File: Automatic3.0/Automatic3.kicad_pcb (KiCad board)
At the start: 2 copper layers, 83 parts, among them J1 CONN_01X02, J10 Encoder, J11 UART0, J12 Bluetooth, J13 Compass, J14 CONN_01X06, J15 I/O PINS, J16 CONN_01X01, J17 CONN_01X01, J18 CONN_01X01, J19 CONN_01X01, J2 CONN_02X04, J3 Motor, J4 Jumper, J5 USB_B, J6 Jumper, J7 Bluetooth, J8 Line Tracker and Proximity, J9 Reset_jumper, SW1 SW_Push, SW2 SW_Push, U1 Buck, U2 LM7809, U3 Arduino_Mega2560_Shield, U4 ATMEGA88A-PU, Y1 Crystal

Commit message: Created new schemetic for automatic
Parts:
- removed C12, C14: C, modFiles:Capacitor_Disc_Medium
- removed C13: 22, modFiles:Capacitor_Disc_Small
- removed J19: CONN_01X01, Connectors:1pin
- removed R23, R26, R27, R28, R29, R30, R31, R32, R33, R34, R35: 10k, modFiles:Resistor_small
- removed Y1: Crystal, modFiles:Crystal
- added C5: 0.1uF, modFiles:Capacitor_Disc_Medium, F.Cu at (326.6, 52.1)
- added D10: D, Diodes_THT:D_DO-27_P12.70mm_Horizontal, F.Cu at (99.8, 62.5)
- added D12: LED, modFiles:LED_D3.0mm, F.Cu at (153.2, 94.0)
- added D13: LED, modFiles:LED_D3.0mm, F.Cu at (94.7, 103.1)
- added R6: 10K, modFiles:Resistor_small, F.Cu at (122.4, 122.7)
- C1: value 1000uF -> 0.1uF; footprint modFiles:Capacitor_1000uF -> modFiles:Capacitor_Disc_Medium
- C10: value 0.1uF -> 10uF; footprint modFiles:Capacitor_Disc_Medium -> modFiles:Capacitor_10uF
- C11, C9: value 0.1uF -> 100uF; footprint modFiles:Capacitor_Disc_Medium -> modFiles:Capacitor_100uF
- C2: value 100uF -> C; footprint modFiles:Capacitor_100uF -> modFiles:Capacitor_Disc_Medium
- C3: value 10uF -> 0.1uF; footprint modFiles:Capacitor_10uF -> modFiles:Capacitor_Disc_Medium
- C4: value 100uF -> 0.1uF; footprint modFiles:Capacitor_100uF -> modFiles:Capacitor_Disc_Medium
- C7: value 22 -> C; footprint modFiles:Capacitor_Disc_Small -> modFiles:Capacitor_Disc_Medium
- C8: value 0.1uF -> 1000uF; footprint modFiles:Capacitor_Disc_Medium -> modFiles:Capacitor_1000uF
- D1: value D -> D_Zener; footprint Diodes_THT:D_DO-27_P12.70mm_Horizontal -> Diodes_THT:D_DO-35_SOD27_P7.62mm_Horizontal
- D11: footprint modFiles:Diode_Small -> Diodes_THT:D_DO-27_P12.70mm_Horizontal
- D2: footprint Diodes_THT:D_DO-27_P12.70mm_Horizontal -> modFiles:Diode_Small
- D3: value LED -> D; footprint modFiles:LED_D3.0mm -> modFiles:Diode_Small
- D4: value LED -> D_Zener; footprint modFiles:LED_D3.0mm -> Diodes_THT:D_DO-35_SOD27_P7.62mm_Horizontal
- D8: value D -> LED; footprint modFiles:Diode_Small -> modFiles:LED_D3.0mm
- D9: value D_Zener -> LED; footprint Diodes_THT:D_DO-35_SOD27_P7.62mm_Horizontal -> modFiles:LED_D3.0mm
- J1: value CONN_01X02 -> I/O PINS; footprint modFiles:Solar_Connector -> Pin_Headers:Pin_Header_Straight_1x03_Pitch2.54mm
- J10: value Encoder -> Line Tracker and Proximity
- J11: value UART0 -> Compass; footprint Pin_Headers:Pin_Header_Straight_1x02_Pitch2.54mm -> Pin_Headers:Pin_Header_Straight_1x04_Pitch2.54mm
- J12: footprint Pin_Headers:Pin_Header_Straight_1x04_Pitch2.54mm -> Pin_Headers:Pin_Header_Straight_1x06_Pitch2.54mm
- J13: value Compass -> Encoder; footprint Pin_Headers:Pin_Header_Straight_1x04_Pitch2.54mm -> modFiles:Connector_DB15
- J14: value CONN_01X06 -> Bluetooth
- J15: value I/O PINS -> Motor; footprint Pin_Headers:Pin_Header_Straight_1x03_Pitch2.54mm -> modFiles:Connector_DB15
- J16: value CONN_01X01 -> CONN_01X02; footprint Connectors:1pin -> modFiles:Solar_Connector
- J17, J18: value CONN_01X01 -> Reset_Jumper; footprint Connectors:1pin -> Pin_Headers:Pin_Header_Straight_1x03_Pitch2.54mm
- J2: value CONN_02X04 -> CONN_01X01; footprint Pin_Headers:Pin_Header_Straight_2x04_Pitch2.54mm -> Connectors:1pin
- J3: value Motor -> CONN_02X04; footprint modFiles:Connector_DB15 -> Pin_Headers:Pin_Header_Straight_2x04_Pitch2.54mm
- J4: value Jumper -> CONN_01X01; footprint Pin_Headers:Pin_Header_Straight_1x02_Pitch2.54mm -> Connectors:1pin
- J5: value USB_B -> CONN_01X01; footprint modFiles:Connector_USB -> Connectors:1pin
- J6: value Jumper -> I/O Pins; footprint Pin_Headers:Pin_Header_Straight_1x02_Pitch2.54mm -> Pin_Headers:Pin_Header_Straight_1x08_Pitch2.54mm
- J7: value Bluetooth -> USB_B; footprint Pin_Headers:Pin_Header_Straight_1x04_Pitch2.54mm -> modFiles:Connector_USB
- J8: value Line Tracker and Proximity -> CONN_01X01; footprint modFiles:Connector_DB15 -> Connectors:1pin
- J9: value Reset_jumper -> I/O Pins; footprint Pin_Headers:Pin_Header_Straight_1x03_Pitch2.54mm -> Pin_Headers:Pin_Header_Straight_1x08_Pitch2.54mm
- R1: value 1K5 -> 1
- R10: footprint Resistors_THT:R_Axial_DIN0207_L6.3mm_D2.5mm_P10.16mm_Horizontal -> modFiles:Resistor_small
- R14: value 10K -> 1K5
- R15, R16, R18, R20: value 10K -> 1K
- R17, R19: value 10K -> 330; footprint modFiles:Resistor_small -> Resistors_THT:R_Axial_DIN0207_L6.3mm_D2.5mm_P10.16mm_Horizontal
- R2, R4: value 1K -> 10K
- R21: value 10K -> 10k
- R22: value 150 -> 10k
- R3: value 330 -> 10K
- R5: value 1 -> 10K
- R8: value 10k -> 10K
- SW1, SW2: value SW_Push -> Reset
- U1: value Buck -> Arduino_Mega2560_Shield; footprint modFiles:Buck_Regulator -> modFiles:Arduino_Mega2560_Shield
- U2: value LM7809 -> Arduino_Mega2560_Shield; footprint modFiles:Voltage_Regulators -> modFiles:Arduino_Mega2560_Shield
- U3: value Arduino_Mega2560_Shield -> Buck; footprint modFiles:Arduino_Mega2560_Shield -> modFiles:Buck_Regulator
- U4: value ATMEGA88A-PU -> LM7809; footprint modFiles:DIP-28 -> modFiles:Voltage_Regulators
- moved C3 243.1 mm to (338.3, 49.8), turned to 0 degrees
- moved C2 233.9 mm to (338.3, 58.4), turned to 0 degrees
- moved C1 224.2 mm to (326.9, 42.4), turned to 0 degrees
- moved R1 206.8 mm to (294.9, 15.0), turned to 0 degrees
- moved J1 189.5 mm to (272.5, 18.0), turned to 0 degrees
- moved C4 181.8 mm to (336.0, 36.3), turned to 0 degrees
- moved C7 177.9 mm to (338.3, 67.6)
- moved J8 141.1 mm to (266.7, 40.9)
- moved C6 138.5 mm to (335.5, 42.4), turned to 0 degrees
- moved J18 128.9 mm to (89.7, 85.1), turned to 0 degrees
- moved J5 114.9 mm to (278.9, 31.0), turned to 0 degrees
- moved J4 109.4 mm to (267.5, 29.5)
- moved J17 100.0 mm to (158.0, 75.7), turned to 0 degrees
- moved R17 93.4 mm to (109.2, 109.5), turned to 0 degrees
- moved D9 92.6 mm to (103.4, 67.6)
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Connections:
- C1 pad 1: /12VV -> GND
- C1 pad 2: GND -> +5V
- C10 pad 1: GND -> +9V
- C10 pad 2: /12VVD -> GND
- C11 pad 1: +9V -> +5V
- C2 pad 1: Net-(C2-Pad1) -> /RESET2
- C3 pad 1: +9V -> GND
- C3 pad 2: GND -> +5V
- C6 pad 1: GND -> +9V
- C6 pad 2: +5V -> GND
- C7 pad 1: Net-(C7-Pad1) -> GND
- C7 pad 2: GND -> /RESET
- C8 pad 1: GND -> /12VV
- C8 pad 2: +5V -> GND
- C9 pad 1: +5V -> Net-(C9-Pad1)
- D1 pad 1: Net-(C2-Pad1) -> /TX2
- D1 pad 2: Net-(D1-Pad2) -> GND
- D11 pad 1: /12VVD -> /12VV
- D11 pad 2: /12VV -> Net-(D11-Pad2)
- D2 pad 1: /12VV -> +5V
- D2 pad 2: /Sheet5ADE4B1B/12led -> +5V
- D3 pad 1: GND -> /12VVD
- D3 pad 2: Net-(D3-Pad2) -> /12VV
- D4 pad 1: GND -> /TX3
- D4 pad 2: Net-(D4-Pad2) -> GND
- D8 pad 1: +5V -> GND
- D8 pad 2: +5V -> Net-(D8-Pad2)
- D9 pad 1: /TX2 -> GND
- D9 pad 2: GND -> Net-(D9-Pad2)
- F1 pad 1: Net-(D1-Pad2) -> Net-(D10-Pad2)
- F2 pad 1: /Sheet5ADE4B1B/12led -> Net-(D11-Pad2)
- J1 pad 1: +12V -> /PB5
- J1 pad 2: GND -> /PB6
- J10 pad 1: /INT2 -> /PC5
- J10 pad 10: /INT4 -> GND
- J10 pad 11: /INT5 -> /12VVD
- J10 pad 12: GND -> /12VVD
- J10 pad 13: +5V -> /JP2
- J10 pad 14: +5V -> /PR1
- J10 pad 15: /PA5 -> /PR2
- J10 pad 2: /INT1 -> /PC7
- J10 pad 3: /INT0 -> /PC6
- J10 pad 4: /PA4 -> /PC4
- J10 pad 5: /PA2 -> /PC2
- J10 pad 6: /PA0 -> /PC0
- J10 pad 7: /PA1 -> /PC1
- J10 pad 8: /PA3 -> /PC3
- J10 pad 9: /INT3 -> /JP1
- J11 pad 1: /TX0 -> +5V
- J11 pad 2: /RX0 -> GND
- J12 pad 1: +5V -> Net-(J12-Pad1)
- J12 pad 2: GND -> +5V
- J12 pad 3: /RX3 -> GND
- J12 pad 4: /TX3 -> /RX2
- J13 pad 1: +5V -> /INT0
- J13 pad 2: GND -> /INT5
- J13 pad 3: Net-(J13-Pad3) -> /INT4
- J13 pad 4: Net-(J13-Pad4) -> /INT3
- J14 pad 2: Net-(J14-Pad2) -> +5V
- J14 pad 3: Net-(J14-Pad3) -> GND
- J14 pad 4: GND -> /RX3
- J14 pad 5: +5V -> /TX3
- J14 pad 6: /RESET2 -> Net-(J14-Pad6)
- J15 pad 1: /PB5 -> /OC5C
- J15 pad 2: /PB6 -> /OC5B
- J15 pad 3: /PB7 -> /PK0
- J16 pad 1: Net-(J16-Pad1) -> +12V
- J17 pad 1: Net-(J17-Pad1) -> /5VV
- J18 pad 1: Net-(J18-Pad1) -> /5VV
- J2 pad 1: +5V -> Net-(J2-Pad1)
- J3 pad 1: /PK7 -> +5V
- J3 pad 2: /PK6 -> GND
- J3 pad 3: /PK5 -> +5V
- J3 pad 4: /PK4 -> GND
- J3 pad 5: /PK3 -> +5V
- J3 pad 6: /PK2 -> GND
- J3 pad 7: /PK1 -> +5V
- J3 pad 8: /OC4A -> GND
- J6 pad 2: /TX2 -> Net-(J6-Pad2)
- J7 pad 1: +5V -> Net-(J7-Pad1)
- J7 pad 2: GND -> /TX3
- J7 pad 3: /RX2 -> /RX3
- J7 pad 4: /TX2 -> GND
- J8 pad 1: /JP1 -> Net-(J8-Pad1)
- J9 pad 1: GND -> Net-(J9-Pad1)
- J9 pad 3: /3V3 -> Net-(J9-Pad3)
- R1 pad 1: Net-(D3-Pad2) -> GND
- R1 pad 2: /Sheet5ADE4B1B/12led -> GND
- R10 pad 1: +5V -> /INT4
- R10 pad 2: /PA0 -> +5V
- R11 pad 1: /INT1 -> +5V
- R11 pad 2: +5V -> /PA4
- R12 pad 1: +5V -> /INT5
- R12 pad 2: /PA1 -> +5V
- R13 pad 1: /INT2 -> +5V
- R13 pad 2: +5V -> /PA5
- R14 pad 1: +5V -> Net-(D5-Pad2)
- R14 pad 2: /PA2 -> +12V
- R15 pad 1: Net-(J9-Pad2) -> Net-(D6-Pad2)
- R15 pad 2: /RESET -> +9V
- R16 pad 1: /INT3 -> Net-(D7-Pad2)
- R16 pad 2: +5V -> +9V
- R17 pad 1: +5V -> Net-(D8-Pad2)
- R17 pad 2: /PA3 -> +5V
- R18 pad 1: /INT4 -> Net-(D9-Pad2)
- R18 pad 2: +5V -> /12VV
- R19 pad 1: +5V -> Net-(D12-Pad2)
- R19 pad 2: /PA4 -> /5VV
- R2 pad 1: Net-(D4-Pad2) -> /INT0
- R2 pad 2: +9V -> +5V
- R20 pad 1: /INT5 -> Net-(D13-Pad2)
- R20 pad 2: +5V -> /5VV
- R21 pad 1: +5V -> Net-(J17-Pad2)
- R21 pad 2: /PA5 -> /RESET1
- R22 pad 1: Net-(D7-Pad2) -> Net-(J18-Pad2)
- R22 pad 2: /3V3 -> /RESET2
- R3 pad 1: Net-(D5-Pad2) -> +5V
- R3 pad 2: +5V -> /PA0
- R4 pad 1: Net-(D6-Pad2) -> /INT1
- R4 pad 2: /12VV -> +5V
- R5 pad 1: GND -> +5V
- R5 pad 2: GND -> /PA1
- R7 pad 2: /RESET2 -> /PA2
- R8 pad 1: +5V -> /INT3
- R8 pad 2: Net-(J13-Pad4) -> +5V
- R9 pad 1: /INT0 -> +5V
- R9 pad 2: +5V -> /PA3
- SW1 pad 2: /RESET2 -> /RESET1
- SW2 pad 2: /RESET -> /RESET2
- U1 pad 3: +5V -> /INT5
- U1 pad 4: GND -> Net-(U1-Pad4)
- U2 pad 1: Net-(C2-Pad1) -> Net-(U2-Pad1)
- U2 pad 2: GND -> /INT4
- U2 pad 3: +9V -> /INT
- U3 pad 1: /TX0 -> /12VV
- U3 pad 2: /INT4 -> GND
- U3 pad 3: /INT5 -> +5V
- U4 pad 1: /RESET2 -> Net-(C9-Pad1)
- U4 pad 2: Net-(R28-Pad2) -> GND
- U4 pad 3: Net-(R29-Pad2) -> +9V
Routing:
- net /JP2: track 106.7 -> 0.86 mm, vias 2 -> 0
- net +5V: track 222.7 -> 120.4 mm
- net /12VVD: track 44.4 -> 127.7 mm
- net /RX2: track 73.2 -> 0.00 mm
- net /TX2: track 72.8 -> 0.00 mm
- net GND: track 78.0 -> 8.44 mm, vias 2 -> 0
- net /JP1: track 11.8 -> 80.8 mm
- net /PB0: track 64.7 -> 0.00 mm
- net /5VV: track 0.00 -> 53.9 mm
- net /INT0: track 14.4 -> 67.6 mm
- net /PA0: track 18.6 -> 69.5 mm
- net /RESET2: track 66.0 -> 19.4 mm
- net /PK0: track 0.00 -> 44.7 mm
- net /PA5: track 32.8 -> 73.5 mm
- net /PC5: track 0.00 -> 36.1 mm, vias 0 -> 2
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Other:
- net class Default: clearance 0.25 -> 0.2; trace_width 1 -> 0.25; via_dia 2.1 -> 0.6; via_drill 0.8 -> 0.4
- rule trace_clearance: 0.25 -> 0.2
- board text removed: "4A K1 K2 K3 K4 K5 K6 K7"
- board text removed: "5V"
- board text removed: "9V"
- board text removed: "A3 A1 A0 A2 A4 I0 I1 I2"
- board text removed: "A5 V V G I5 I4 I3"
- board text removed: "ABU ROBOCON 2018"
- board text removed: "ABU ROBOCON 2018 AUTOMATIC BASE"
- board text removed: "ANT"
- board text removed: "ARDUINO RESET"
- board text removed: "ATMEGA RESET"
- board text removed: "B0 G G G 5A 5C 5B"
- board text removed: "B7 B6 B5"
- board text removed: "BUCK"
- board text removed: "DO--D7 , B0,B1 F0--F7 , G1,D7"
- board text removed: "G R2 T2 -"
- board text removed: "MEGA"
- board text removed: "R2 G G G V V V"
- board text removed: "RST VCC GND SCK MISO MOSI"
- board text removed: "T2 R2 G V"
- board text removed: "T2 R3 T3 G J2 P1 P2 J1"
- board text removed: "T3"
- board text removed: "V G CL DA"
- board text removed: "V R G"

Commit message: Modified the automatic circuit
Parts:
- removed C4: 0.1uF, modFiles:Capacitor_Disc_Medium
- removed J1: I/O PINS, Pin_Headers:Pin_Header_Straight_1x03_Pitch2.54mm
- added C12: 104, modFiles:Capacitor_Disc_Medium, F.Cu at (138.5, 110.5)
- added C15: 104, modFiles:Capacitor_Disc_Medium, F.Cu at (58.1, 77.0)
- added C16: 104, modFiles:Capacitor_Disc_Medium, F.Cu at (139.8, 85.6)
- added C17: 104, modFiles:Capacitor_Disc_Medium, F.Cu at (83.6, 143.8)
- added R23: 10k, modFiles:Resistor_small, F.Cu at (150.5, 77.4)
- added R24: 10k, modFiles:Resistor_small, F.Cu at (153.9, 77.3)
- C1, C3, C5, C6: value 0.1uF -> 104
- C2, C7: value C -> 104
- D12, D13, D8: value LED -> LED_5V
- D5: value LED -> LED_12V
- D6, D7: value LED -> LED_9V
- D9: value LED -> LED_BUCK
- J3: value CONN_02X04 -> GND VCC
- R17, R19: footprint Resistors_THT:R_Axial_DIN0207_L6.3mm_D2.5mm_P10.16mm_Horizontal -> modFiles:Resistor_small
- moved C3 277.2 mm to (61.5, 63.8), turned to 180 degrees
- moved C2 257.7 mm to (84.5, 102.9), turned to 180 degrees
- moved J5 257.3 mm to (43.5, 134.8)
- moved J8 222.5 mm to (44.3, 39.6)
- moved C5 221.7 mm to (124.8, 143.7), turned to 270 degrees
- moved C7 215.5 mm to (123.0, 59.9), turned to 180 degrees
- moved C1 208.1 mm to (121.1, 73.4), turned to 180 degrees
- moved C6 194.7 mm to (142.7, 69.8), turned to 270 degrees
- moved R1 169.5 mm to (158.3, 115.3)
- moved J2 144.6 mm to (168.3, 135.2)
- moved J4 100.5 mm to (167.5, 39.9)
- moved R16 42.5 mm to (123.3, 76.8), turned to 180 degrees
- moved J3 41.2 mm to (125.9, 93.6), turned to 180 degrees
- moved R19 38.0 mm to (139.3, 72.0)
- moved D7 38.0 mm to (131.0, 75.6)
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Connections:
- net /INT3 renamed /SINT3
- net /INT4 renamed /SINT4
- C1 pad 2: +5V -> +9V
- C2 pad 1: /RESET2 -> +5V
- C3 pad 2: +5V -> /RESET2
- C6 pad 1: +9V -> +5V
- C7 pad 2: /RESET -> /RESET1
- D4 pad 1: /TX3 -> /TX1
- J13 pad 1: /INT0 -> /INT2
- J13 pad 5: /INT2 -> /SINT2
- J13 pad 6: /INT1 -> /SINT5
- J14 pad 4: /RX3 -> /INT2
- J14 pad 5: /TX3 -> /TX1
- J2 pad 1: Net-(J2-Pad1) -> GND
- J4 pad 1: Net-(J4-Pad1) -> GND
- J5 pad 1: Net-(J5-Pad1) -> GND
- J7 pad 2: /TX3 -> /RX3
- J7 pad 3: /RX3 -> /TX3
- J8 pad 1: Net-(J8-Pad1) -> GND
- R2 pad 1: /INT0 -> /INT2
- R4 pad 1: /INT1 -> /SINT5
- R6 pad 1: /INT2 -> /SINT2
- U1 pad 18: Net-(U1-Pad18) -> /TX1
- U1 pad 19: Net-(U1-Pad19) -> /INT2
- U2 pad 10: Net-(U2-Pad10) -> /INT
- U2 pad 19: /INT2 -> /SINT2
- U2 pad 3: /INT -> /SINT5
- U2 pad GND5: Net-(U2-PadGND5) -> GND
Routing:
- net +5V: track 120.4 -> 374.7 mm, vias 0 -> 2
- net GND: track 8.44 -> 200.6 mm
- net /SDA: track 0.74 -> 105.2 mm, vias 0 -> 2
- net /SCL: track 0.00 -> 87.2 mm
- net +9V: track 61.1 -> 138.2 mm, vias 0 -> 2
- net /INT2: track 36.0 -> 110.9 mm
- net /JP2: track 0.86 -> 69.5 mm, vias 0 -> 2
- net /INT0: track 67.6 -> 0.00 mm
- net /SINT5: track 0.00 -> 67.0 mm
- net /TX1: track 0.00 -> 57.9 mm
- net /RX2: track 0.00 -> 47.5 mm
- net /INT: track 28.3 -> 71.0 mm
- net /SINT2: track 0.00 -> 36.0 mm
- net /INT1: track 32.9 -> 0.00 mm
- net /TX2: track 0.00 -> 25.3 mm
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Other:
- board text added: "#MASTER"
- board text added: "#SLAVE"
- board text added: "- R3 T3 G"
- board text added: "A1 A3 5V 5V G A5 A0"
- board text added: "A2 A4 I5 I2 I3 I4 MI5 MI2"
- board text added: "ABU_ROBOCON_2018"
- board text added: "ANT"
- board text added: "Automatic Base"
- board text added: "BUCK_FUSE"
- board text added: "C3 C1 C0 C2 C4 C6 C7 C5"
- board text added: "F0 F1 F2 F3 F4 F5 F6 F7"
- board text added: "K5 K4 K3 K2 K1 K0 5B 5C"
- board text added: "K7 K6 G-G-G 4A 5A"
- board text added: "LED BUCK"
- board text added: "MEGA_FUSE"
- board text added: "P2 P1 J2 12 12 G J1"
- board text added: "POWER"
- board text added: "RESET"
- board text added: "TX1 RX1 GND VCC"
- board text added: "TX2 RX2 GND VCC"
- board text added: "V R G"
- board text added: "VCC GND SCL SDA"

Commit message: modified the automatic circuit
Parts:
- removed J3: GND VCC, Pin_Headers:Pin_Header_Straight_2x04_Pitch2.54mm
- added D14: LED, modFiles:LED_D3.0mm, F.Cu at (166.3, 47.7)
- added D15: D_Zener, Diodes_THT:D_DO-35_SOD27_P7.62mm_Horizontal, F.Cu at (92.1, 94.5)
- added D16: LED, modFiles:LED_D3.0mm, F.Cu at (168.2, 52.7)
- added D17: LED, modFiles:LED_D3.0mm, F.Cu at (164.1, 52.8)
- added J1: CONN_02X05, Pin_Headers:Pin_Header_Straight_2x05_Pitch2.54mm, F.Cu at (123.3, 84.4)
- added J19: Bluetooth, Pin_Headers:Pin_Header_Straight_1x06_Pitch2.54mm, F.Cu at (94.8, 107.5)
- added R25: 1, modFiles:Resistor_small, F.Cu at (84.0, 99.3)
- added R26: 1, modFiles:Resistor_small, F.Cu at (84.3, 109.0)
- added R27: 1, modFiles:Resistor_small, F.Cu at (121.7, 106.9)
- added R28: R, modFiles:Resistor_small, F.Cu at (169.7, 57.9)
- added R29: R, modFiles:Resistor_small, F.Cu at (166.5, 57.9)
- added R30: R, modFiles:Resistor_small, F.Cu at (163.5, 57.9)
- D7: value LED_9V -> LED
- moved R1 81.8 mm to (94.4, 64.2), turned to 270 degrees
- moved R4 29.0 mm to (96.4, 87.2)
- moved D1 28.2 mm to (127.5, 112.3)
- moved C16 17.2 mm to (131.8, 100.9), turned to 270 degrees
- moved D4 14.3 mm to (153.9, 95.6), turned to 270 degrees
- moved C12 13.5 mm to (149.6, 102.7), turned to 90 degrees
- moved J14 12.8 mm to (146.4, 101.3)
- moved J12 8.48 mm to (135.7, 101.4)
- moved R22 6.61 mm to (63.6, 71.6)
- moved D3 6.29 mm to (70.0, 101.8)
- moved R17 6.19 mm to (75.9, 103.6)
- moved R15 5.83 mm to (59.8, 88.3)
- moved D8 5.49 mm to (79.1, 95.4), turned to 0 degrees
- moved C2 5.07 mm to (80.0, 100.5)
- moved C15 4.77 mm to (54.1, 74.5), turned to 270 degrees
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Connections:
- D4 pad 1: /TX1 -> /TX0
- J14 pad 4: /INT2 -> /RX0
- J14 pad 5: /TX1 -> /TX0
- R1 pad 1: GND -> /12VV
- R1 pad 2: GND -> /INT
- U1 pad A15: Net-(U1-PadA15) -> /JP2
- U1 pad A8: /JP2 -> /INT
- U2 pad 14: Net-(U2-Pad14) -> /STX3
- U2 pad 15: Net-(U2-Pad15) -> /SRX3
- U2 pad 16: Net-(U2-Pad16) -> /RX2
- U2 pad 17: Net-(U2-Pad17) -> /TX2
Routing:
- net GND: track 200.6 -> 303.6 mm
- net /TX2: track 25.3 -> 111.9 mm, vias 0 -> 2
- net /TX1: track 57.9 -> 0.00 mm
- net /INT2: track 110.9 -> 73.2 mm
- net /RX2: track 47.5 -> 82.8 mm, vias 0 -> 2
- net +5V: track 374.7 -> 405.1 mm, vias 2 -> 4
- net /12VV: track 62.6 -> 86.1 mm
- net /RX0: track 0.00 -> 19.1 mm
- net /JP2: track 69.5 -> 50.6 mm
- net /TX0: track 0.00 -> 18.5 mm
- net /INT: track 71.0 -> 53.1 mm
- net +9V: track 138.2 -> 122.2 mm
- net /5VV: track 64.4 -> 49.9 mm
- net Net-(R28-Pad2): track 0.00 -> 12.4 mm
- net Net-(D14-Pad2): track 0.00 -> 11.9 mm
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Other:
- board text added: "Bluetooth"
- board text added: "TX3 RX3 GND VCC"
- board text added: "UART0"
- board text added: "UART2"

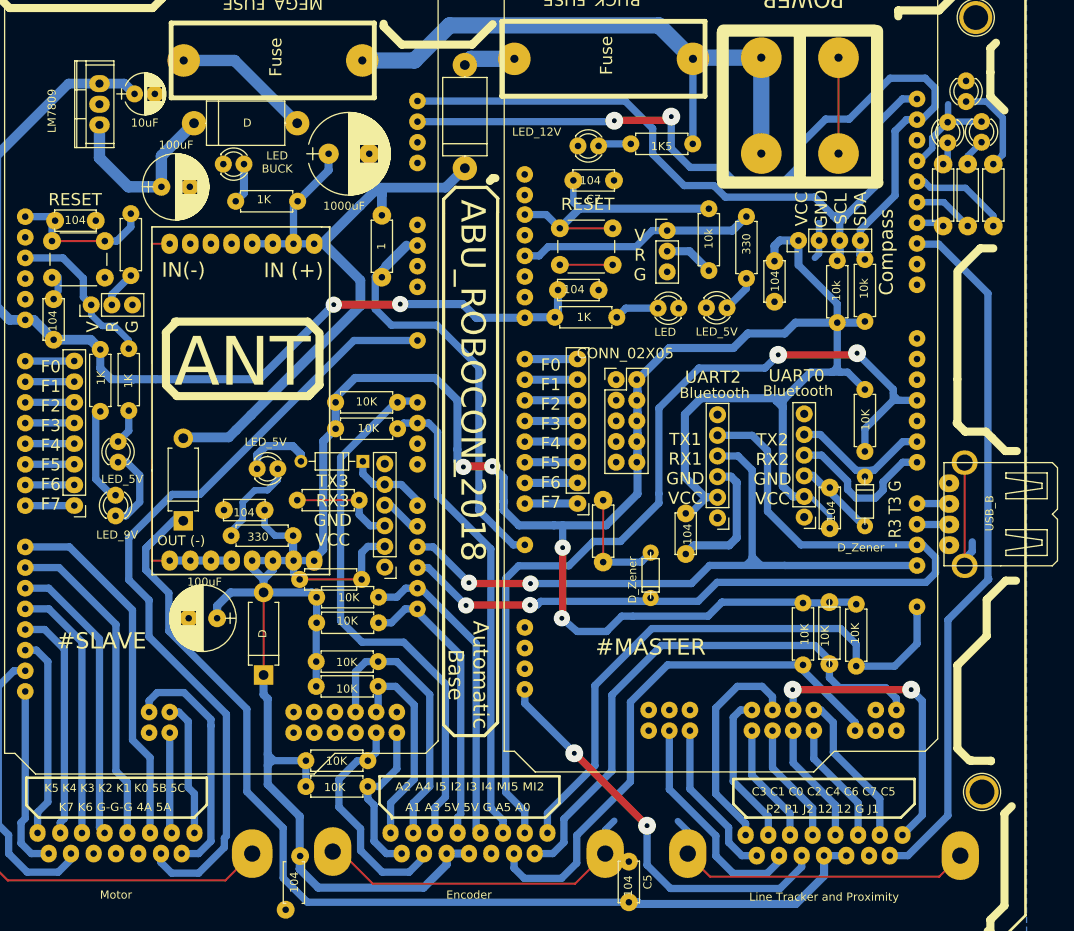
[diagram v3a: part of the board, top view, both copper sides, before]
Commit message: added the jst connector
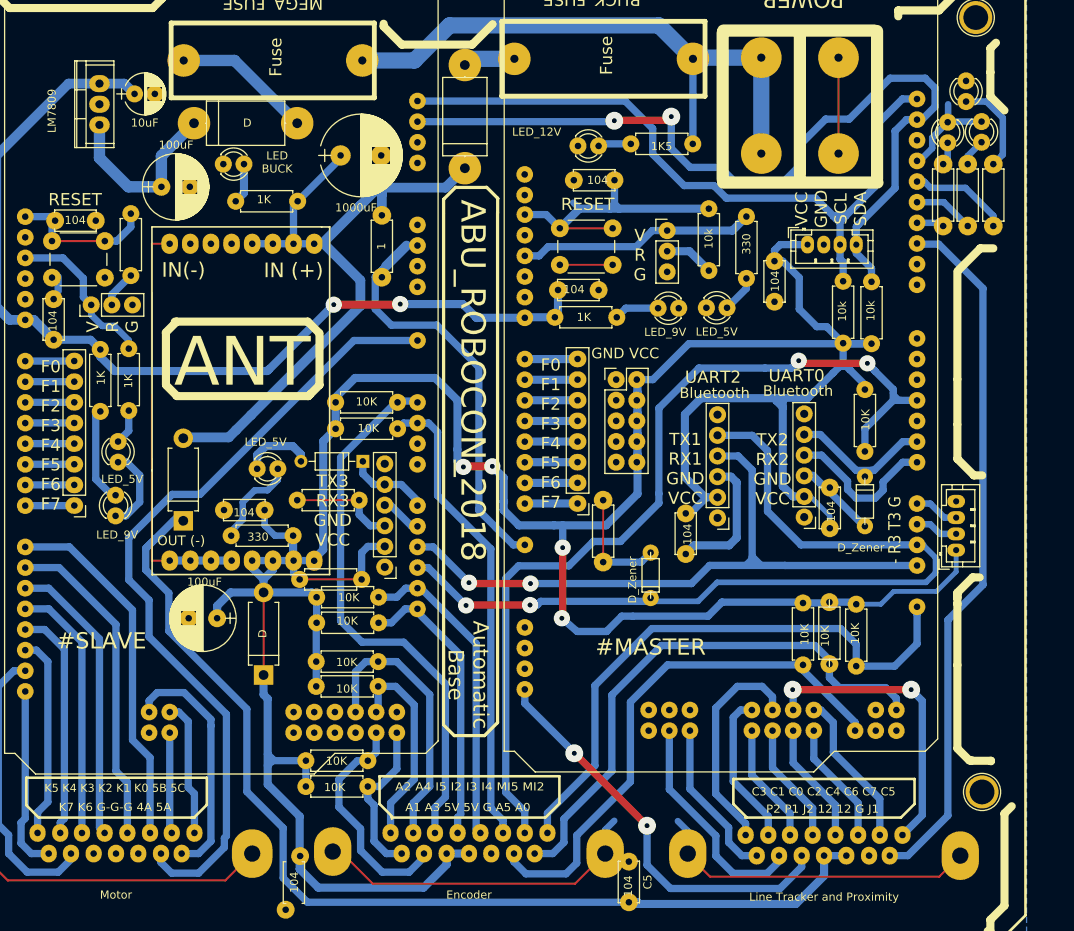
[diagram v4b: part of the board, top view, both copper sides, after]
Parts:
- D7: value LED -> LED_9V
- J1: value CONN_02X05 -> GND VCC
- J11: footprint Pin_Headers:Pin_Header_Straight_1x04_Pitch2.54mm -> Connectors_JST:JST_PH_B4B-PH-K_04x2.00mm_Straight
- J7: footprint modFiles:Connector_USB -> Connectors_JST:JST_PH_B4B-PH-K_04x2.00mm_Straight
- moved J7 7.05 mm to (165.1, 105.4), turned to 90 degrees
- moved C7 4.94 mm to (118.1, 59.9), turned to 0 degrees
- moved R24 2.86 mm to (154.7, 80.0)
- moved R23 2.63 mm to (151.2, 79.9)
- moved C8 1.49 mm to (89.4, 56.8)
- moved J11 1.23 mm to (146.8, 67.8), turned to 0 degrees
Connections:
- J7 pad 1: Net-(J7-Pad1) -> +5V
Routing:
- net GND: track 303.6 -> 281.6 mm
- net +5V: track 405.1 -> 425.2 mm
- net /TX2: track 111.9 -> 107.9 mm
- net /SDA: track 104.0 -> 107.5 mm
- net /RESET1: track 35.7 -> 38.3 mm
- net /SCL: track 87.2 -> 89.7 mm
- net +9V: track 122.2 -> 120.5 mm
- net /TX3: track 4.02 -> 5.53 mm
- net /RX3: track 4.02 -> 5.36 mm
- net /PA5: track 67.2 -> 66.3 mm
- net /JP1: track 87.5 -> 86.7 mm
- net /INT5: track 114.0 -> 113.3 mm
